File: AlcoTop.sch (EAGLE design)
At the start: 26 parts, among them IC4 ATMEGA328, Y1 16MHz

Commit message: Added transistor switch for MQ3 and pushbutton to change mode. 100mA operating current. YAY
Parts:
- added PB1: (no value), SparkFun-Connectors:M02LOCK_LONGPADS
- added Q1: (no value), SparkFun-DiscreteSemi:TRANSISTOR_NPNTO-92-AMMO
- added R5: 10K, Dek:RESISTORAXIAL-0.3
- added R6: 120, Dek:RESISTORAXIAL-0.3
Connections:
- new net MQ3: MQ3R.1, Q1.C
- new net N$5: IC4.(ADC5)PC5
- new net N$7: Q1.B, R6.1
- net D12: now also R6.2
- net GND: now also Q1.E, R5.2; no longer MQ3R.1
- net SCL: now also PB1.1, R5.1; no longer IC4.(ADC5)PC5
- net VCC: now also PB1.2
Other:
- note added: "MQ3 Breakout Headers"
- note added: "MQ3 Power Control"
- note added: "Mode Pushbutton"
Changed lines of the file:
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@@
 <part name="P+6" library="SparkFun" deviceset="VCC" device=""/>
 <part name="R4" library="Dek" deviceset="RESISTOR" device="AXIAL-0.3" value="10K"/>
+<part name="PB1" library="SparkFun-Connectors" deviceset="M02" device="LOCK_LONGPADS"/>
+<part name="R5" library="Dek" deviceset="RESISTOR" device="AXIAL-0.3" value="10K"/>
+<part name="GND8" library="SparkFun" deviceset="GND" device=""/>
+<part name="P+7" library="SparkFun" deviceset="VCC" device=""/>
+<part name="Q1" library="SparkFun-DiscreteSemi" deviceset="TRANSISTOR_NPN" device="TO-92-AMMO"/>
+<part name="R6" library="Dek" deviceset="RESISTOR" device="AXIAL-0.3" value="120"/>
 <part name="GND7" library="SparkFun" deviceset="GND" device=""/>
 </parts>
@@
 <plain>
 <text x="43.18" y="76.2" size="2.54" layer="94">MCU</text>
-<text x="86.36" y="203.2" size="2.54" layer="94" rot="R180">FTDI Header</text>
+<text x="86.36" y="203.2" size="1.778" layer="94" rot="R180">FTDI Header</text>
+<text x="119.38" y="139.7" size="1.778" layer="94" rot="R180">Mode Pushbutton</text>
+<text x="121.92" y="91.44" size="1.778" layer="94" rot="R180">MQ3 Power Control</text>
+<text x="-12.7" y="78.74" size="1.778" layer="94" rot="R180">MQ3 Breakout Headers</text>
 </plain>
 <instances>
@@
 </instance>
 <instance part="R4" gate="G$1" x="-20.32" y="104.14" rot="R90"/>
-<instance part="GND7" gate="1" x="-15.24" y="96.52" rot="R90"/>
+<instance part="PB1" gate="G$1" x="116.84" y="149.86" rot="R180"/>
+<instance part="R5" gate="G$1" x="106.68" y="157.48" rot="R90"/>
+<instance part="GND8" gate="1" x="106.68" y="165.1" rot="R180"/>
+<instance part="P+7" gate="1" x="104.14" y="147.32" rot="R90"/>
+<instance part="Q1" gate="G$1" x="116.84" y="106.68"/>
+<instance part="R6" gate="G$1" x="109.22" y="106.68" rot="R180"/>
+<instance part="GND7" gate="1" x="119.38" y="96.52"/>
 </instances>
 <busses>
@@
 </segment>
 <segment>
-<pinref part="MQ3R" gate="G$1" pin="1"/>
+<pinref part="R5" gate="G$1" pin="2"/>
+<pinref part="GND8" gate="1" pin="GND"/>
+</segment>
+<segment>
+<pinref part="Q1" gate="G$1" pin="E"/>
 <pinref part="GND7" gate="1" pin="GND"/>
-<wire x1="-17.78" y1="96.52" x2="-17.78" y2="91.44" width="0.1524" layer="91"/>
+<wire x1="119.38" y1="99.06" x2="119.38" y2="101.6" width="0.1524" layer="91"/>
 </segment>
 </net>
@@
 <wire x1="-33.02" y1="91.44" x2="-33.02" y2="93.98" width="0.1524" layer="91"/>
 </segment>
+<segment>
+<pinref part="PB1" gate="G$1" pin="2"/>
+<pinref part="P+7" gate="1" pin="VCC"/>
+<wire x1="104.14" y1="147.32" x2="109.22" y2="147.32" width="0.1524" layer="91"/>
+</segment>
 </net>
 <net name="D6" class="0">
@@
 <pinref part="IC4" gate="G$1" pin="(MISO)PB4"/>
 </segment>
+<segment>
+<pinref part="R6" gate="G$1" pin="2"/>
+<wire x1="104.14" y1="106.68" x2="99.06" y2="106.68" width="0.1524" layer="91"/>
+<label x="99.06" y="106.68" size="1.778" layer="95"/>
+</segment>
 </net>
 <net name="D2" class="0">
@@
 <net name="SCL" class="0">
 <segment>
-<wire x1="68.58" y1="121.92" x2="76.2" y2="121.92" width="0.1524" layer="91"/>
 <label x="71.12" y="121.92" size="1.778" layer="95"/>
-<pinref part="IC4" gate="G$1" pin="(ADC5)PC5"/>
+<pinref part="PB1" gate="G$1" pin="1"/>
+<wire x1="109.22" y1="149.86" x2="106.68" y2="149.86" width="0.1524" layer="91"/>
+<pinref part="R5" gate="G$1" pin="1"/>
+<wire x1="106.68" y1="152.4" x2="106.68" y2="149.86" width="0.1524" layer="91"/>
+<wire x1="106.68" y1="149.86" x2="101.6" y2="149.86" width="0.1524" layer="91"/>
+<junction x="106.68" y="149.86"/>
+<label x="101.6" y="149.86" size="1.778" layer="95"/>
 </segment>
 </net>
@@
 </segment>
 </net>
+<net name="N$5" class="0">
+<segment>
+<pinref part="IC4" gate="G$1" pin="(ADC5)PC5"/>
+<wire x1="68.58" y1="121.92" x2="76.2" y2="121.92" width="0.1524" layer="91"/>
+</segment>
+</net>
+<net name="N$7" class="0">
+<segment>
+<pinref part="Q1" gate="G$1" pin="B"/>
+<pinref part="R6" gate="G$1" pin="1"/>
+</segment>
+</net>
+<net name="MQ3" class="1">
+<segment>
+<pinref part="MQ3R" gate="G$1" pin="1"/>
+<wire x1="-17.78" y1="96.52" x2="-17.78" y2="91.44" width="0.1524" layer="91"/>
+<label x="-17.78" y="96.52" size="1.778" layer="95" rot="R270"/>
+</segment>
+<segment>
+<pinref part="Q1" gate="G$1" pin="C"/>
+<wire x1="119.38" y1="111.76" x2="119.38" y2="119.38" width="0.1524" layer="91"/>
+<label x="116.84" y="119.38" size="1.778" layer="95" rot="R270"/>
+</segment>
+</net>

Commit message: Updated board
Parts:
- removed JP5: STAND-OFF#2, Dek:STAND-OFF#2
- removed PB1: (no value), SparkFun-Connectors:M02LOCK_LONGPADS
- added MODE: (no value), Dek:M02LOCK_LONGPADS
- BATT, MQ3L, MQ3R, PWR_SW: device SparkFun-Connectors:M02LOCK_LONGPADS -> Dek:M02LOCK_LONGPADS
- D1: value (none) -> 1N4001; device Dek:DIODE1N4148 -> Dek:DIODEPTH
- IC2: value (none) -> 7805; device SparkFun-PowerIC:V_REG_78XXSINK -> Dek:V_REG_78XXSINK
- IC4: device atmel:AT90S4433P -> Dek:AT90S4433P
- LED1, LED2: device SparkFun-LED:LED5MM -> Dek:LED5MM
- LED_STRIP: device SparkFun-Connectors:M04LOCK_LONGPADS -> Dek:M04LOCK_LONGPADS
- Y1: device SparkFun:CRYSTALHC49US -> Dek:CRYSTALHC49US
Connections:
- removed net SCL: PB1.1, R5.1
- net D2: now also MODE.1, R5.1; no longer LED_STRIP.1
- net D3: now also LED2.A; no longer LED_STRIP.2
- net D7: now also LED_STRIP.1; no longer LED2.A
- net D8: now also LED_STRIP.2
- net VCC: now also MODE.2; no longer PB1.2
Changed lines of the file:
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@@
 </classes>
 <parts>
-<part name="IC4" library="atmel" deviceset="AT90S4433" device="P" value="ATMEGA328"/>
-<part name="Y1" library="SparkFun" deviceset="CRYSTAL" device="HC49US" value="16MHz"/>
+<part name="IC4" library="Dek" deviceset="AT90S4433" device="P" value="ATMEGA328"/>
+<part name="Y1" library="Dek" deviceset="CRYSTAL" device="HC49US" value="16MHz"/>
 <part name="C9" library="Dek" deviceset="CAP" device="PTH2" value="22pF"/>
 <part name="C14" library="Dek" deviceset="CAP" device="PTH2" value="22pF"/>
@@
 <part name="C2" library="Dek" deviceset="CAP_POL" device="PTH2" value="0.33uF"/>
 <part name="C1" library="Dek" deviceset="CAP" device="PTH2" value="0.1uF"/>
-<part name="D1" library="Dek" deviceset="DIODE" device="1N4148"/>
+<part name="D1" library="Dek" deviceset="DIODE" device="PTH" value="1N4001"/>
 <part name="JP1" library="Dek" deviceset="STAND-OFF" device="#2"/>
 <part name="JP2" library="Dek" deviceset="STAND-OFF" device="#2"/>
 <part name="JP6" library="Dek" deviceset="STAND-OFF" device="#2"/>
-<part name="JP5" library="Dek" deviceset="STAND-OFF" device="#2"/>
-<part name="LED1" library="SparkFun-LED" deviceset="LED" device="5MM"/>
+<part name="LED1" library="Dek" deviceset="LED" device="5MM"/>
 <part name="R1" library="Dek" deviceset="RESISTOR" device="AXIAL-0.3" value="1K"/>
 <part name="P+1" library="SparkFun" deviceset="VCC" device=""/>
 <part name="GND1" library="SparkFun" deviceset="GND" device=""/>
-<part name="BATT" library="SparkFun-Connectors" deviceset="M02" device="LOCK_LONGPADS"/>
-<part name="PWR_SW" library="SparkFun-Connectors" deviceset="M02" device="LOCK_LONGPADS"/>
+<part name="BATT" library="Dek" deviceset="M02" device="LOCK_LONGPADS"/>
+<part name="PWR_SW" library="Dek" deviceset="M02" device="LOCK_LONGPADS"/>
 <part name="GND2" library="SparkFun" deviceset="GND" device=""/>
-<part name="LED_STRIP" library="SparkFun-Connectors" deviceset="M04" device="LOCK_LONGPADS"/>
+<part name="LED_STRIP" library="Dek" deviceset="M04" device="LOCK_LONGPADS"/>
 <part name="GND3" library="SparkFun" deviceset="GND" device=""/>
 <part name="P+4" library="SparkFun" deviceset="VCC" device=""/>
-<part name="IC2" library="SparkFun-PowerIC" deviceset="V_REG_78XX" device="SINK"/>
-<part name="LED2" library="SparkFun-LED" deviceset="LED" device="5MM"/>
+<part name="IC2" library="Dek" deviceset="V_REG_78XX" device="SINK" value="7805"/>
+<part name="LED2" library="Dek" deviceset="LED" device="5MM"/>
 <part name="R2" library="Dek" deviceset="RESISTOR" device="AXIAL-0.3" value="1K"/>
 <part name="GND4" library="SparkFun" deviceset="GND" device=""/>
-<part name="MQ3L" library="SparkFun-Connectors" deviceset="M02" device="LOCK_LONGPADS"/>
-<part name="MQ3R" library="SparkFun-Connectors" deviceset="M02" device="LOCK_LONGPADS"/>
+<part name="MQ3L" library="Dek" deviceset="M02" device="LOCK_LONGPADS"/>
+<part name="MQ3R" library="Dek" deviceset="M02" device="LOCK_LONGPADS"/>
 <part name="GND6" library="SparkFun" deviceset="GND" device=""/>
 <part name="P+5" library="SparkFun" deviceset="VCC" device=""/>
 <part name="P+6" library="SparkFun" deviceset="VCC" device=""/>
 <part name="R4" library="Dek" deviceset="RESISTOR" device="AXIAL-0.3" value="10K"/>
-<part name="PB1" library="SparkFun-Connectors" deviceset="M02" device="LOCK_LONGPADS"/>
+<part name="MODE" library="Dek" deviceset="M02" device="LOCK_LONGPADS"/>
 <part name="R5" library="Dek" deviceset="RESISTOR" device="AXIAL-0.3" value="10K"/>
 <part name="GND8" library="SparkFun" deviceset="GND" device=""/>
@@
 <instance part="JP2" gate="G$1" x="12.7" y="86.36"/>
 <instance part="JP6" gate="G$1" x="12.7" y="83.82"/>
-<instance part="JP5" gate="G$1" x="10.16" y="83.82"/>
 <instance part="LED1" gate="G$1" x="27.94" y="172.72" rot="R90"/>
 <instance part="R1" gate="G$1" x="43.18" y="172.72" rot="R180"/>
@@
 </instance>
 <instance part="R4" gate="G$1" x="-20.32" y="104.14" rot="R90"/>
-<instance part="PB1" gate="G$1" x="116.84" y="149.86" rot="R180"/>
+<instance part="MODE" gate="G$1" x="116.84" y="149.86" rot="R180"/>
 <instance part="R5" gate="G$1" x="106.68" y="157.48" rot="R90"/>
 <instance part="GND8" gate="1" x="106.68" y="165.1" rot="R180"/>
@@
 </segment>
 <segment>
-<pinref part="PB1" gate="G$1" pin="2"/>
+<pinref part="MODE" gate="G$1" pin="2"/>
 <pinref part="P+7" gate="1" pin="VCC"/>
 <wire x1="104.14" y1="147.32" x2="109.22" y2="147.32" width="0.1524" layer="91"/>
@@
 </segment>
 <segment>
+<pinref part="MODE" gate="G$1" pin="1"/>
+<pinref part="R5" gate="G$1" pin="1"/>
+<wire x1="109.22" y1="149.86" x2="106.68" y2="149.86" width="0.1524" layer="91"/>
+<wire x1="106.68" y1="149.86" x2="106.68" y2="152.4" width="0.1524" layer="91"/>
+<wire x1="106.68" y1="149.86" x2="101.6" y2="149.86" width="0.1524" layer="91"/>
+<junction x="106.68" y="149.86"/>
+<label x="101.6" y="149.86" size="1.778" layer="95"/>
+</segment>
+</net>
+<net name="SDA" class="0">
+<segment>
+<wire x1="68.58" y1="119.38" x2="76.2" y2="119.38" width="0.1524" layer="91"/>
+<label x="71.12" y="119.38" size="1.778" layer="95"/>
+<pinref part="IC4" gate="G$1" pin="(ADC4)PC4"/>
+</segment>
+</net>
+<net name="D5" class="0">
+<segment>
+<wire x1="68.58" y1="99.06" x2="76.2" y2="99.06" width="0.1524" layer="91"/>
+<label x="71.12" y="99.06" size="1.778" layer="95"/>
+<pinref part="IC4" gate="G$1" pin="(T1)PD5"/>
+</segment>
+</net>
+<net name="D13" class="0">
+<segment>
+<wire x1="68.58" y1="139.7" x2="76.2" y2="139.7" width="0.1524" layer="91"/>
+<label x="71.12" y="139.7" size="1.778" layer="95"/>
+<pinref part="IC4" gate="G$1" pin="(SCK)PB5"/>
+</segment>
+</net>
+<net name="D7" class="0">
+<segment>
+<wire x1="68.58" y1="104.14" x2="76.2" y2="104.14" width="0.1524" layer="91"/>
+<label x="71.12" y="104.14" size="1.778" layer="95"/>
+<pinref part="IC4" gate="G$1" pin="(AIN1)PD7"/>
+</segment>
+<segment>
 <pinref part="LED_STRIP" gate="G$1" pin="1"/>
 <wire x1="-27.94" y1="165.1" x2="-17.78" y2="165.1" width="0.1524" layer="91"/>
@@
 </segment>
 </net>
-<net name="SCL" class="0">
-<segment>
-<label x="71.12" y="121.92" size="1.778" layer="95"/>
-<pinref part="PB1" gate="G$1" pin="1"/>
-<wire x1="109.22" y1="149.86" x2="106.68" y2="149.86" width="0.1524" layer="91"/>
-<pinref part="R5" gate="G$1" pin="1"/>
-<wire x1="106.68" y1="152.4" x2="106.68" y2="149.86" width="0.1524" layer="91"/>
-<wire x1="106.68" y1="149.86" x2="101.6" y2="149.86" width="0.1524" layer="91"/>
-<junction x="106.68" y="149.86"/>
-<label x="101.6" y="149.86" size="1.778" layer="95"/>
-</segment>
-</net>
-<net name="SDA" class="0">
-<segment>
-<wire x1="68.58" y1="119.38" x2="76.2" y2="119.38" width="0.1524" layer="91"/>
-<label x="71.12" y="119.38" size="1.778" layer="95"/>
-<pinref part="IC4" gate="G$1" pin="(ADC4)PC4"/>
-</segment>
-</net>
-<net name="D5" class="0">
-<segment>
-<wire x1="68.58" y1="99.06" x2="76.2" y2="99.06" width="0.1524" layer="91"/>
-<label x="71.12" y="99.06" size="1.778" layer="95"/>
-<pinref part="IC4" gate="G$1" pin="(T1)PD5"/>
-</segment>
-</net>
-<net name="D13" class="0">
-<segment>
-<wire x1="68.58" y1="139.7" x2="76.2" y2="139.7" width="0.1524" layer="91"/>
-<label x="71.12" y="139.7" size="1.778" layer="95"/>
-<pinref part="IC4" gate="G$1" pin="(SCK)PB5"/>
-</segment>
-</net>
-<net name="D7" class="0">
-<segment>
-<wire x1="68.58" y1="104.14" x2="76.2" y2="104.14" width="0.1524" layer="91"/>
-<label x="71.12" y="104.14" size="1.778" layer="95"/>
-<pinref part="IC4" gate="G$1" pin="(AIN1)PD7"/>
-</segment>
-<segment>
-<pinref part="LED2" gate="G$1" pin="A"/>
-<wire x1="17.78" y1="165.1" x2="25.4" y2="165.1" width="0.1524" layer="91"/>
-<label x="17.78" y="165.1" size="1.778" layer="95"/>
-</segment>
-</net>
 <net name="D3" class="0">
 <segment>
@@
 </segment>
 <segment>
-<pinref part="LED_STRIP" gate="G$1" pin="2"/>
-<wire x1="-27.94" y1="167.64" x2="-17.78" y2="167.64" width="0.1524" layer="91"/>
-<label x="-20.32" y="165.1" size="1.778" layer="95"/>
+<pinref part="LED2" gate="G$1" pin="A"/>
+<wire x1="25.4" y1="165.1" x2="17.78" y2="165.1" width="0.1524" layer="91"/>
+<label x="17.78" y="165.1" size="1.778" layer="95"/>
 </segment>
 </net>
@@
 <pinref part="IC4" gate="G$1" pin="(ICP)PB0"/>
 </segment>
-</net>
+<segment>
+<pinref part="LED_STRIP" gate="G$1" pin="2"/>
+<wire x1="-27.94" y1="167.64" x2="-17.78" y2="167.64" width="0.1524" layer="91"/>
+<label x="-20.32" y="165.1" size="1.778" layer="95"/>
+</segment>
+</net>

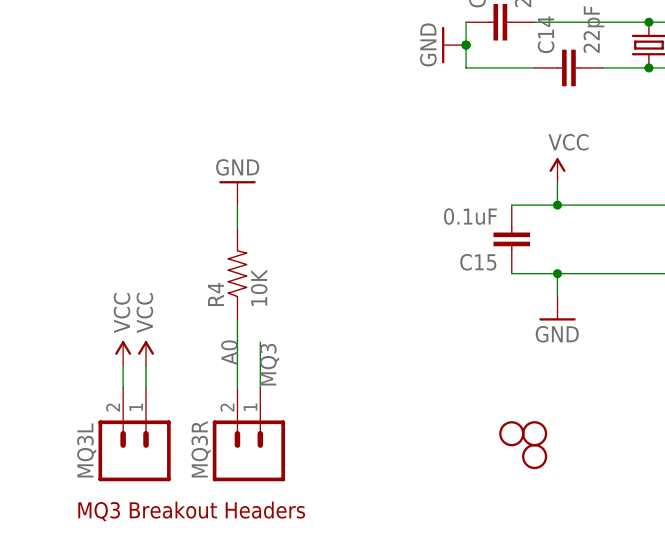
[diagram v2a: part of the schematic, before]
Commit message: Reduced MQ3 voltage divider resistor to 1K
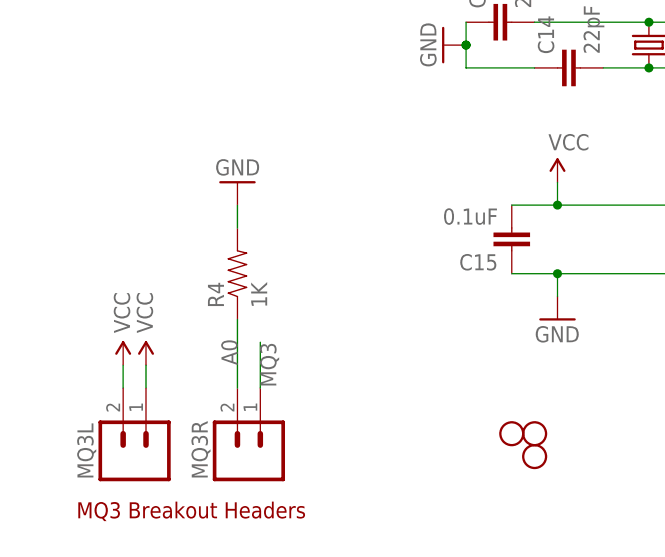
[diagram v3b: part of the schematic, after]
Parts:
- R4: value 10K -> 1K
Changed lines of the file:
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@@
 <part name="P+5" library="SparkFun" deviceset="VCC" device=""/>
 <part name="P+6" library="SparkFun" deviceset="VCC" device=""/>
-<part name="R4" library="Dek" deviceset="RESISTOR" device="AXIAL-0.3" value="10K"/>
+<part name="R4" library="Dek" deviceset="RESISTOR" device="AXIAL-0.3" value="1K"/>
 <part name="MODE" library="Dek" deviceset="M02" device="LOCK_LONGPADS"/>
 <part name="R5" library="Dek" deviceset="RESISTOR" device="AXIAL-0.3" value="10K"/>
